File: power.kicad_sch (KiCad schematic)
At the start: 16 parts, among them U1 AP2112K-3.3, U2 TPS7A20xxxDBV

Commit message: add decoupling pins
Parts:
- added C10, C12, C14, C16, C18, C20, C22, C23: 100nF, symbol Device:C
- added C11, C13, C15, C17, C19: 4.7uF, symbol Device:C
- added C21, C27: 1uF, symbol Device:C
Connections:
- net +3.3V: now also C10.1, C11.1, C12.1, C13.1, C14.1, C15.1, C16.1, C17.1, C18.1, C19.1
- net +3.3VA: now also C20.1, C21.1, C22.1, C23.1, C27.1
- net GND: now also C10.2, C11.2, C12.2, C13.2, C14.2, C15.2, C16.2, C17.2, C18.2, C19.2
- net GNDA: now also C20.2, C21.2, C22.2, C23.2, C27.2
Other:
- note added: "1 pair per pin (5 VDD pins)"
- note added: "VBAT Decoupling"
- note added: "VDD Decoupling"
- note added: "VDDA Decoupling"
- note added: "VREF Decoupling"
- moved on the sheet: C1, C2, C3, C4, C5, C6, C7, C8, C9, D1, F1, FB1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

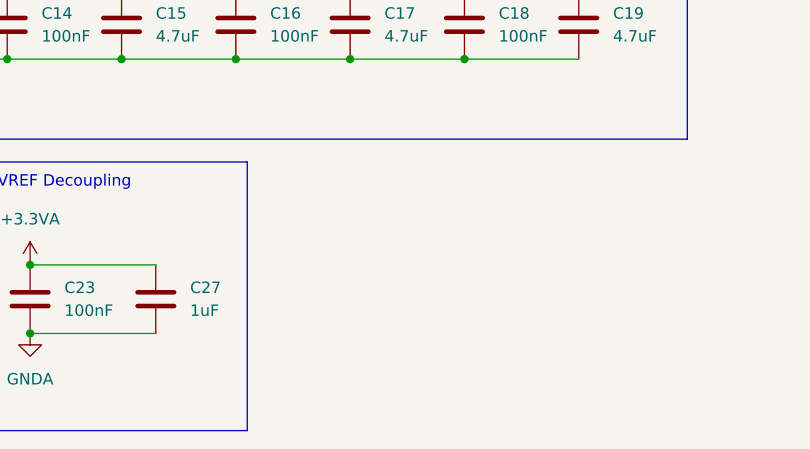
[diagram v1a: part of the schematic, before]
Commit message: add sensors and muxes
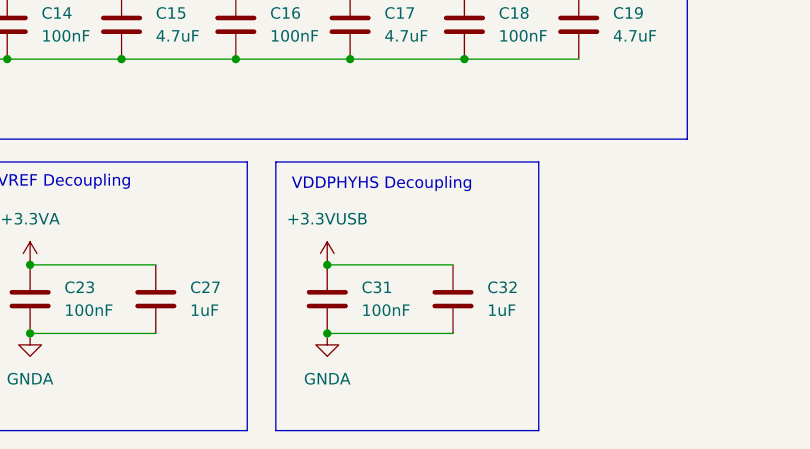
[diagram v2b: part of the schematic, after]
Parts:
- added C31: 100nF, symbol Device:C
- added C32: 1uF, symbol Device:C
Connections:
- net +3.3VUSB: now also C31.1, C32.1
- net GNDA: now also C31.2, C32.2
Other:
- note added: "VDDPHYHS Decoupling"
